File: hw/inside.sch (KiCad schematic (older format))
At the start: 23 parts

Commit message: hw: schematics update with libs
Signed-off-by: Pierre-Yves Kerbrat <pkerbrat@free.fr>
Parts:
- removed TH?: DHT22_TEMPERATURE_HUMIDITY, symbol DHT22_TEMPERATURE_HUMIDITY
- removed U?: ARDUINO_PRO_MINI, symbol ARDUINO_PRO_MINI
- added TH?: DHT22_Temperature_Humidity, symbol DHT22_Temperature_Humidity
- added U?: Arduino_Pro_Mini, symbol Arduino_Pro_Mini
- 10K: symbol R_VARIABLE -> R_Variable
- BT?: symbol BATTERY -> Battery
- SW? (x3): symbol SW_PUSH_DUAL -> SW_Push_Dual
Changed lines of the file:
@@
 EESchema Schematic File Version 2
+LIBS:inside-rescue
 LIBS:power
 LIBS:device
@@
 LIBS:memory
 LIBS:xilinx
-LIBS:special
 LIBS:microcontrollers
 LIBS:dsp
@@
 LIBS:contrib
 LIBS:valves
-LIBS:mq135
+LIBS:maxim
+LIBS:switches
+LIBS:crumpschemes
 LIBS:sensors
-LIBS:crumpschemes
-LIBS:maxim
-LIBS:Arduino_Pro_Mini-cache
-LIBS:switches
+LIBS:misc
+LIBS:nodemcu
 LIBS:inside-cache
-EELAYER 27 0
+EELAYER 25 0
 EELAYER END
 $Descr A4 11693 8268
@@
 Comment4 ""
 $EndDescr
-$Comp
-L DHT22_TEMPERATURE_HUMIDITY TH?
-U 1 1 58FF439D
-P 9900 2250
-F 0 "TH?" H 9900 3300 60  0000 C CNN
-F 1 "DHT22_TEMPERATURE_HUMIDITY" H 9900 3200 60  0000 C CNN
-F 2 "" H 9900 2250 60  0000 C CNN
-F 3 "" H 9900 2250 60  0000 C CNN
-	1    9900 2250
-	1    0    0    -1
-$EndComp
 $Comp
 L LCD16X2 DS?
@@
 $EndComp
 $Comp
-L R_VARIABLE 10K
+L R_Variable 10K
 U 1 1 58FF61D2
 P 3800 5000
@@
 	8850 5700 8850 5950
 Connection ~ 8850 5800
-$Comp
-L ARDUINO_PRO_MINI U?
-U 1 1 58FF7EDC
-P 5800 4850
-F 0 "U?" H 5500 5600 60  0000 C CNN
-F 1 "ARDUINO_PRO_MINI" H 5800 2900 60  0000 C CNN
-F 2 "" H 5800 4850 60  0000 C CNN
-F 3 "" H 5800 4850 60  0000 C CNN
-	1    5800 4850
-	1    0    0    -1
-$EndComp
 Text GLabel 6750 5850 2    60   Input ~ 0
 TH
@@
 Connection ~ 9750 4900
 $Comp
-L BATTERY BT?
+L Battery BT?
 U 1 1 58FF818A
 P 10550 5600
@@
 	550  2800 4550 2800
 $Comp
-L SW_PUSH_DUAL SW?
+L SW_Push_Dual SW?
 U 1 1 58FF9459
 P 5800 2050
@@
 $EndComp
 $Comp
-L SW_PUSH_DUAL SW?
+L SW_Push_Dual SW?
 U 1 1 58FF9477
 P 5800 900
@@
 	6450 2250 6450 2450
 $Comp
-L SW_PUSH_DUAL SW?
+L SW_Push_Dual SW?
 U 1 1 58FF9C10
 P 7500 1450
@@
 Text Notes 5200 3750 2    60   ~ 0
 range 5V-12V
+$Comp
+L Arduino_Pro_Mini U?
+U 1 1 5908F849
+P 5800 4850
+F 0 "U?" H 5500 5600 60  0000 C CNN
+F 1 "Arduino_Pro_Mini" H 5800 2900 60  0000 C CNN
+F 2 "" H 5800 4850 60  0000 C CNN
+F 3 "" H 5800 4850 60  0000 C CNN
+	1    5800 4850
+	1    0    0    -1
+$EndComp
+$Comp
+L DHT22_Temperature_Humidity TH?
+U 1 1 5908FC51
+P 9900 2250
+F 0 "TH?" H 9900 3300 60  0000 C CNN
+F 1 "DHT22_Temperature_Humidity" H 9900 3200 60  0000 C CNN
+F 2 "" H 9900 2250 60  0000 C CNN
+F 3 "" H 9900 2250 60  0000 C CNN
+	1    9900 2250
+	1    0    0    -1
+$EndComp
 $EndSCHEMATC

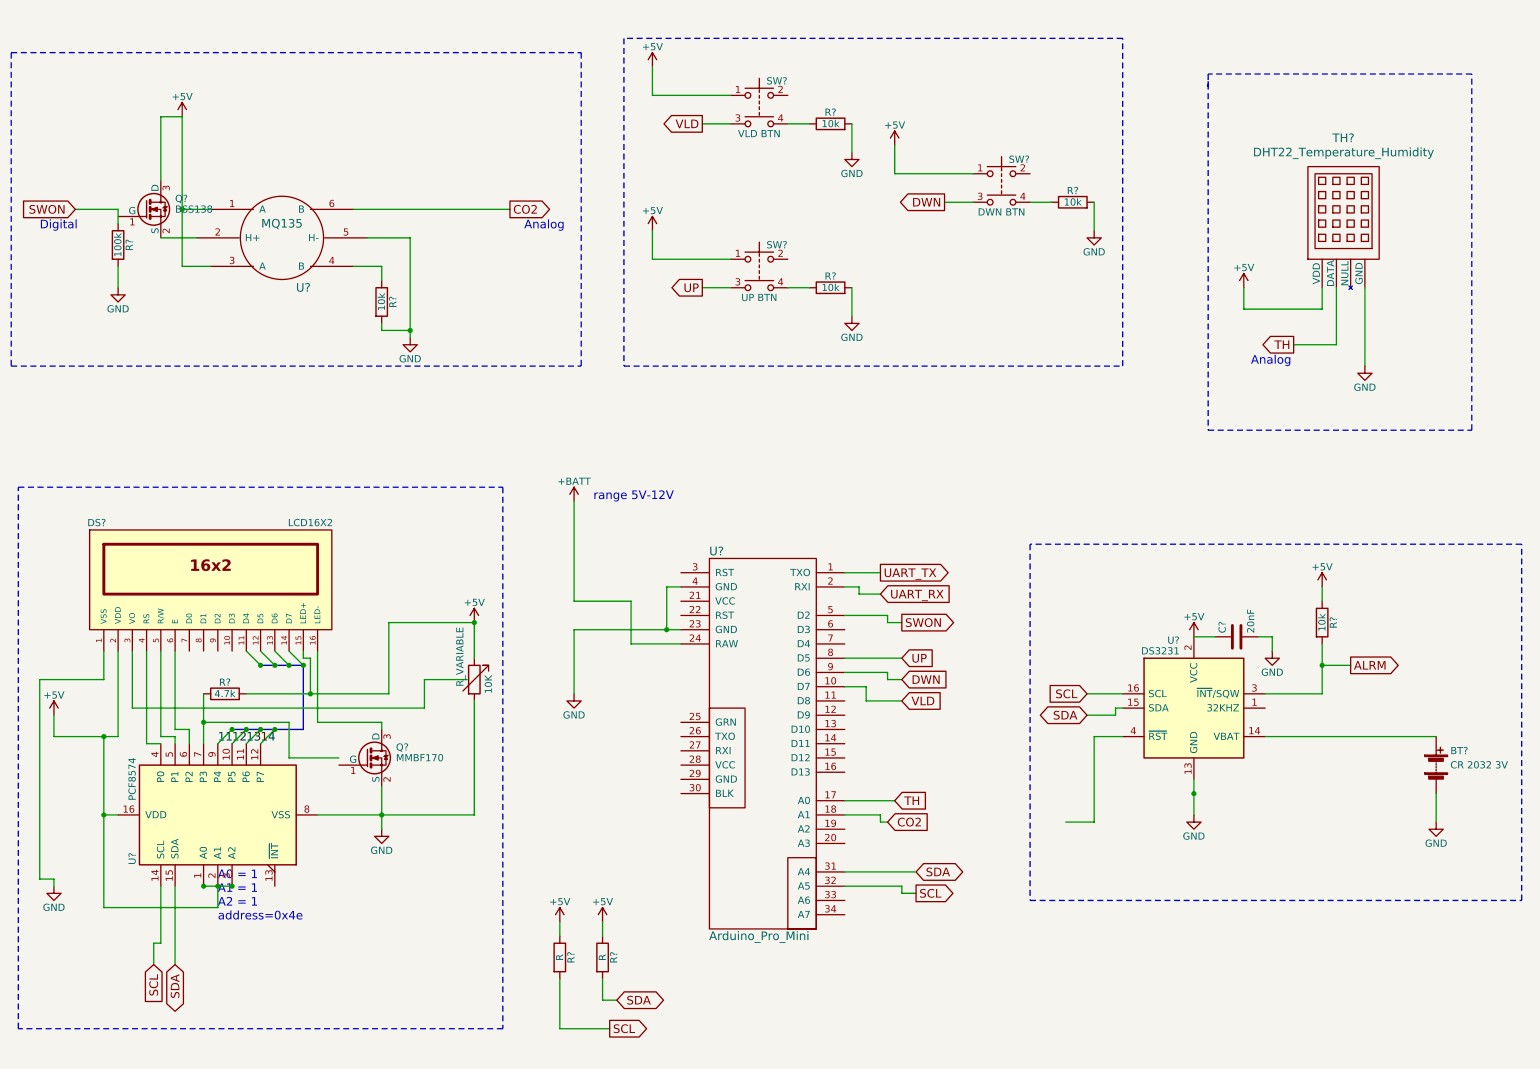
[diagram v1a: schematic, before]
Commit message: hw: add decoupling cap (100nF) to DHT22 and add some text
Signed-off-by: Pierre-Yves Kerbrat <pkerbrat@free.fr>
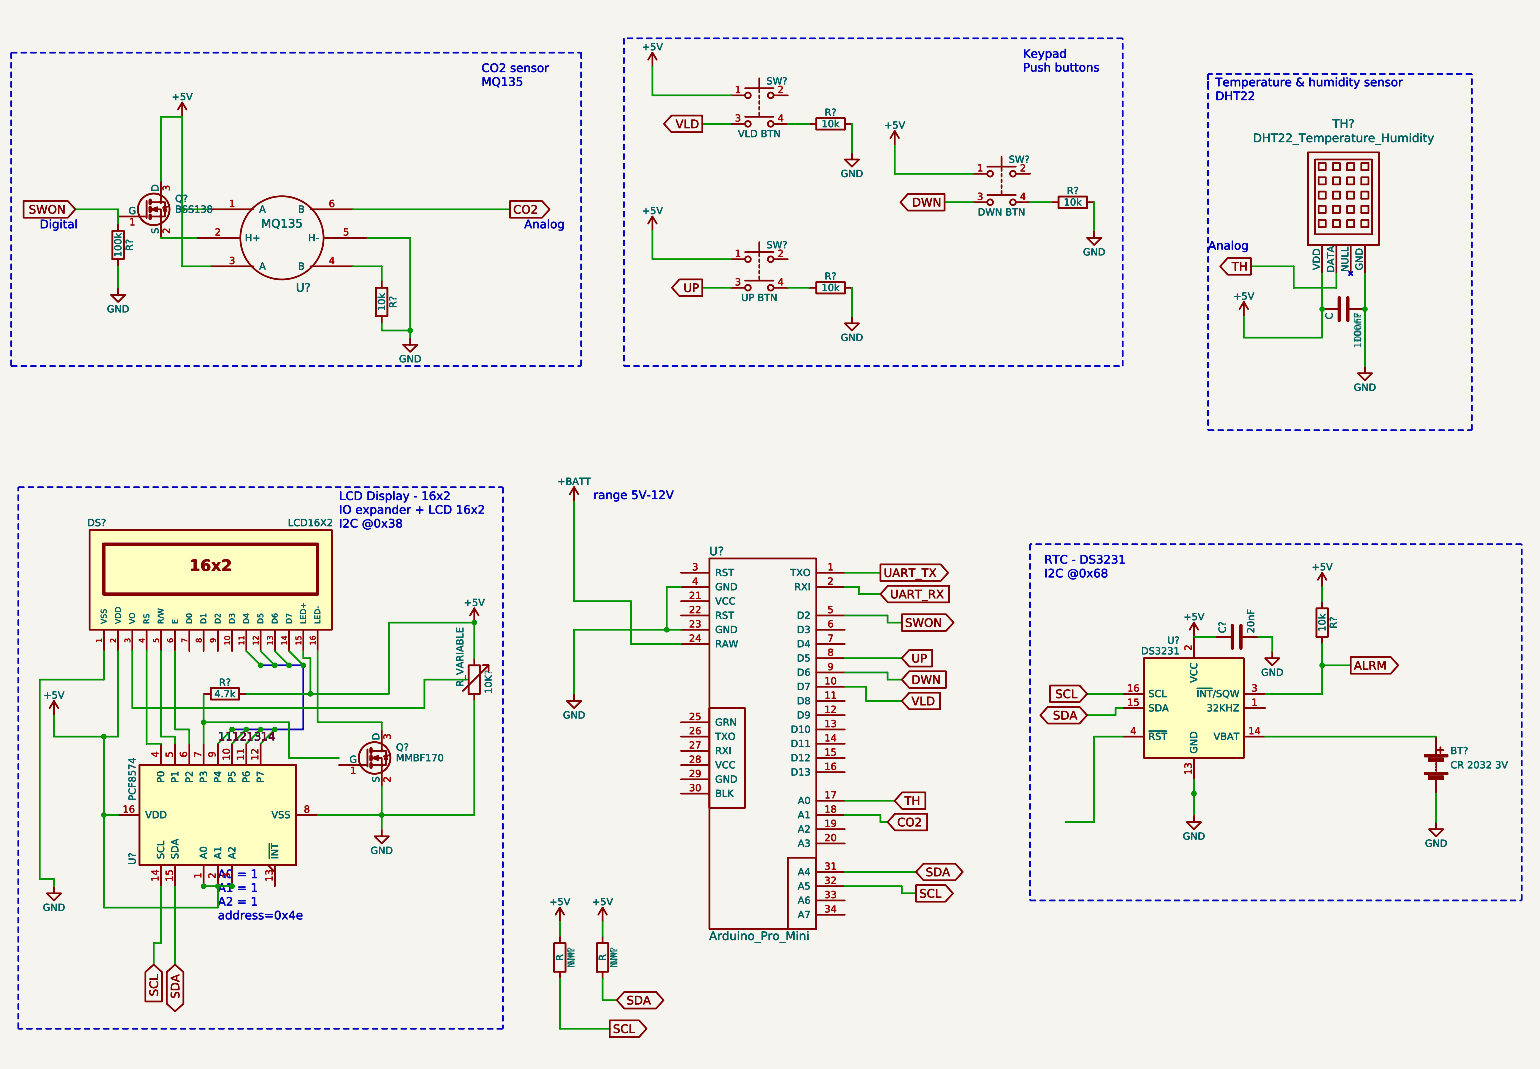
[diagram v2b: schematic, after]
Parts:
- added 100nF, 100nF?: C, symbol C
- added 10K?: R_VARIABLE, symbol R_Variable
- added BT?: CR 2032 3V, symbol Battery
- added C?: 20nF, symbol C
- added DS?: LCD16X2, WC1602A, symbol LCD16X2
- added NM? (x2): R, symbol R
- added Q?: BSS138, TO_SOT_Packages_SMD:SOT-23, symbol BSS138
- added Q?: MMBF170, TO_SOT_Packages_SMD:SOT-23, symbol MMBF170
- added R? (x5): 10k, symbol R
- added R?: 100k, symbol R
- added R?: 4.7k, symbol R
- added SW?: UP BTN, symbol SW_Push_Dual
- added SW?: VLD BTN, symbol SW_Push_Dual
- added SW?: DWN BTN, symbol SW_Push_Dual
- added TH?: DHT22_Temperature_Humidity, symbol DHT22_Temperature_Humidity
- added U?: MQ135, ~, symbol MQ135
- added U?: PCF8574, symbol PCF8574
- added U?: DS3231, Housings_SOIC:SOIC-16_7.5x10.3mm_Pitch1.27mm, symbol DS3231
- added U?: Arduino_Pro_Mini, symbol Arduino_Pro_Mini
- gave numbers to parts that had none: 1
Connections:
- net +5V: now also 100nF.2, 100nF?.2, 10K?.1, C?.1, DS?.15 (LED+), DS?.2 (VDD), NM?.1, NM?.1, Q?.3 (D), R?.1, R?.2, SW?.1, SW?.1, SW?.1, TH?.1 (VDD), U?.1 (A), U?.1 (A0), U?.16 (VDD), U?.2 (A1), U?.2 (VCC), U?.3 (A), U?.3 (A2)
- net +BATT: now also U?.24 (RAW)
- net 11: now also U?.9 (P4)
- net 12: now also U?.10 (P5)
- net 13: now also U?.11 (P6)
- net 14: now also U?.12 (P7)
- net ALRM: now also R?.2, U?.3 (~INT~/SQW)
- net CO2: now also U?.18 (A1), U?.6 (B)
- net DWN: now also SW?.3, U?.9 (D6)
- net GND: now also 100nF.1, 100nF?.1, 10K?.2, BT?.2 (-), C?.2, DS?.1 (VSS), Q?.2 (S), R?.2, R?.2, R?.2, R?.2, R?.2, TH?.4 (GND), U?.10 (NC), U?.11 (NC), U?.12 (NC), U?.13 (GND), U?.23 (GND), U?.4 (GND), U?.5 (H-), U?.5 (NC), U?.6 (NC), U?.7 (NC), U?.8 (NC), U?.8 (VSS), U?.9 (NC)
- net SCL: now also NM?.2, U?.14 (SCL), U?.16 (SCL), U?.32 (A5)
- net SDA: now also NM?.2, U?.15 (SDA), U?.15 (SDA), U?.31 (A4)
- net SWON: now also R?.1, U?.5 (D2)
- net TH: now also TH?.2 (DATA), U?.17 (A0)
- net UART_RX: now also U?.2 (RXI)
- net UART_TX: now also U?.1 (TXO)
- net UP: now also SW?.3, U?.8 (D5)
- net VLD: now also SW?.3, U?.10 (D7)
- net at DS?.10 (D3): now also DS?.10 (D3)
- net at DS?.11 (D4): now also DS?.11 (D4)
- net at DS?.12 (D5): now also DS?.12 (D5)
- net at DS?.13 (D6): now also DS?.13 (D6)
- net at DS?.14 (D7): now also DS?.14 (D7)
- net at DS?.16 (LED-), Q?.3 (D): now also DS?.16 (LED-), Q?.3 (D)
- net at DS?.3 (VO): now also DS?.3 (VO)
- net at DS?.4 (RS), U?.4 (P0): now also DS?.4 (RS), U?.4 (P0)
- net at DS?.5 (R/W), U?.5 (P1): now also DS?.5 (R/W), U?.5 (P1)
- net at DS?.6 (E), U?.6 (P2): now also DS?.6 (E), U?.6 (P2)
- net at DS?.7 (D0): now also DS?.7 (D0)
- net at DS?.8 (D1): now also DS?.8 (D1)
- net at DS?.9 (D2): now also DS?.9 (D2)
- net at Q?.2 (S), U?.2 (H+): now also Q?.2 (S), U?.2 (H+)
- net at R?.1, U?.4 (B): now also R?.1, U?.4 (B)
- net at Q?.1 (G): now also Q?.1 (G) (x2)
- net at U?.13 (~INT~): now also U?.13 (~INT~)
- net at R?.1, U?.7 (P3): now also R?.1, U?.7 (P3)
- net at U?.1 (32KHZ): now also U?.1 (32KHZ)
- net at BT?.1 (+), U?.14 (VBAT): now also BT?.1 (+), U?.14 (VBAT)
- net at U?.4 (~RST): now also U?.4 (~RST)
- net at SW?.2: now also SW?.2 (x3)
- net at R?.1, SW?.4: now also R?.1, SW?.4 (x3)
- net at U?.11 (D8): now also U?.11 (D8)
- net at U?.12 (D9): now also U?.12 (D9)
- net at U?.13 (D10): now also U?.13 (D10)
- net at U?.14 (D11): now also U?.14 (D11)
- net at U?.15 (D12): now also U?.15 (D12)
- net at U?.16 (D13): now also U?.16 (D13)
- net at U?.19 (A2): now also U?.19 (A2)
- net at U?.20 (A3): now also U?.20 (A3)
- net at U?.21 (VCC): now also U?.21 (VCC)
- net at U?.22 (RST): now also U?.22 (RST)
- net at U?.25 (GRN): now also U?.25 (GRN)
- net at U?.26 (TXO): now also U?.26 (TXO)
- net at U?.27 (RXI): now also U?.27 (RXI)
- net at U?.28 (VCC): now also U?.28 (VCC)
- net at U?.29 (GND): now also U?.29 (GND)
- net at U?.3 (RST): now also U?.3 (RST)
- net at U?.30 (BLK): now also U?.30 (BLK)
- net at U?.33 (A6): now also U?.33 (A6)
- net at U?.34 (A7): now also U?.34 (A7)
- net at U?.6 (D3): now also U?.6 (D3)
- net at U?.7 (D4): now also U?.7 (D4)
- net at TH?.3 (NULL): now also TH?.3 (NULL)
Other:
- note added: "CO2 sensor\nMQ135"
- note added: "Keypad\nPush buttons"
- note added: "LCD Display - 16x2\nIO expander + LCD 16x2\nI2C @0x38"
- note added: "RTC - DS3231\nI2C @0x68"
- note added: "Temperature & humidity sensor\nDHT22"
- moved on the sheet: TH?

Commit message: hw: annotate schematics
Signed-off-by: Pierre-Yves Kerbrat <pkerbrat@free.fr>
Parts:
- removed 100nF: C, symbol C
- removed 10K: R_VARIABLE, symbol R_Variable
- removed BT?: CR 2032 3V, symbol Battery
- removed C?: 20nF, symbol C
- removed DS?: LCD16X2, WC1602A, symbol LCD16X2
- removed NM (x2): R, symbol R
- removed Q?: BSS138, TO_SOT_Packages_SMD:SOT-23, symbol BSS138
- removed Q?: MMBF170, TO_SOT_Packages_SMD:SOT-23, symbol MMBF170
- removed R? (x5): 10k, symbol R
- removed R?: 100k, symbol R
- removed R?: 4.7k, symbol R
- removed SW?: UP BTN, symbol SW_Push_Dual
- removed SW?: VLD BTN, symbol SW_Push_Dual
- removed SW?: DWN BTN, symbol SW_Push_Dual
- removed TH?: DHT22_Temperature_Humidity, symbol DHT22_Temperature_Humidity
- removed U?: MQ135, ~, symbol MQ135
- removed U?: PCF8574, symbol PCF8574
- removed U?: Arduino_Pro_Mini, symbol Arduino_Pro_Mini
- removed U?: DS3231, Housings_SOIC:SOIC-16_7.5x10.3mm_Pitch1.27mm, symbol DS3231
- gave numbers to parts that had none: 24
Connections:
- net TH: now also U3.6 (D3); no longer U3.17 (A0)
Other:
- note added: "A0 = 1\nA1 = 1\nA2 = 1\naddress=0x38"
- note removed: "A0 = 1\nA1 = 1\nA2 = 1\naddress=0x4e"

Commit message: hw: fix errors
Signed-off-by: Pierre-Yves Kerbrat <pkerbrat@free.fr>
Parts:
- removed 10K1: R_VARIABLE, symbol R_Variable
- added 10K1: POT, symbol POT
- added P1, P2: CONN_01X02, symbol CONN_01X02
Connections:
- net +5V: now also 10K1.1
- net +BATT: now also P2.1 (P1)
- net GND: now also 10K1.3, P2.2 (P2)
- net SWON: now also Q1.1 (G)
- net UART_RX: now also P1.2 (P2)
- net UART_TX: now also P1.1 (P1)
- net at DS1.3 (VO): now also 10K1.2
- net at R2.1, U1.7 (P3): now also Q2.1 (G)
- net ALRM: no longer names the net of R7.2, U4.3 (~INT~/SQW)
- no-connect marks 0 -> 31
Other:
- moved on the sheet: 100nF1, BT1, C1, R7, TH1, U4
